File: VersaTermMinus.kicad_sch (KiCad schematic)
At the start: 55 parts, among them CN1 HDMI_A, CN2 DE15_Socket, CN3 USB_B_Micro, CN5 USB_B_Micro, CN6 Mini-DIN-6, CN7 TTL Serial, CN8 DE9 Socket, J2 USBDATA, Q1 2N7002, Q2 2N7002, Q3 2N7002, Q4 2N7002, Q5 2N7002, Q6 2N7002, Q7 2N7002, SW1 RESET, SW2 DEFAULTS, SW3 3V3/5V, U1 Raspberry Pi Pico, U3 MAX3232

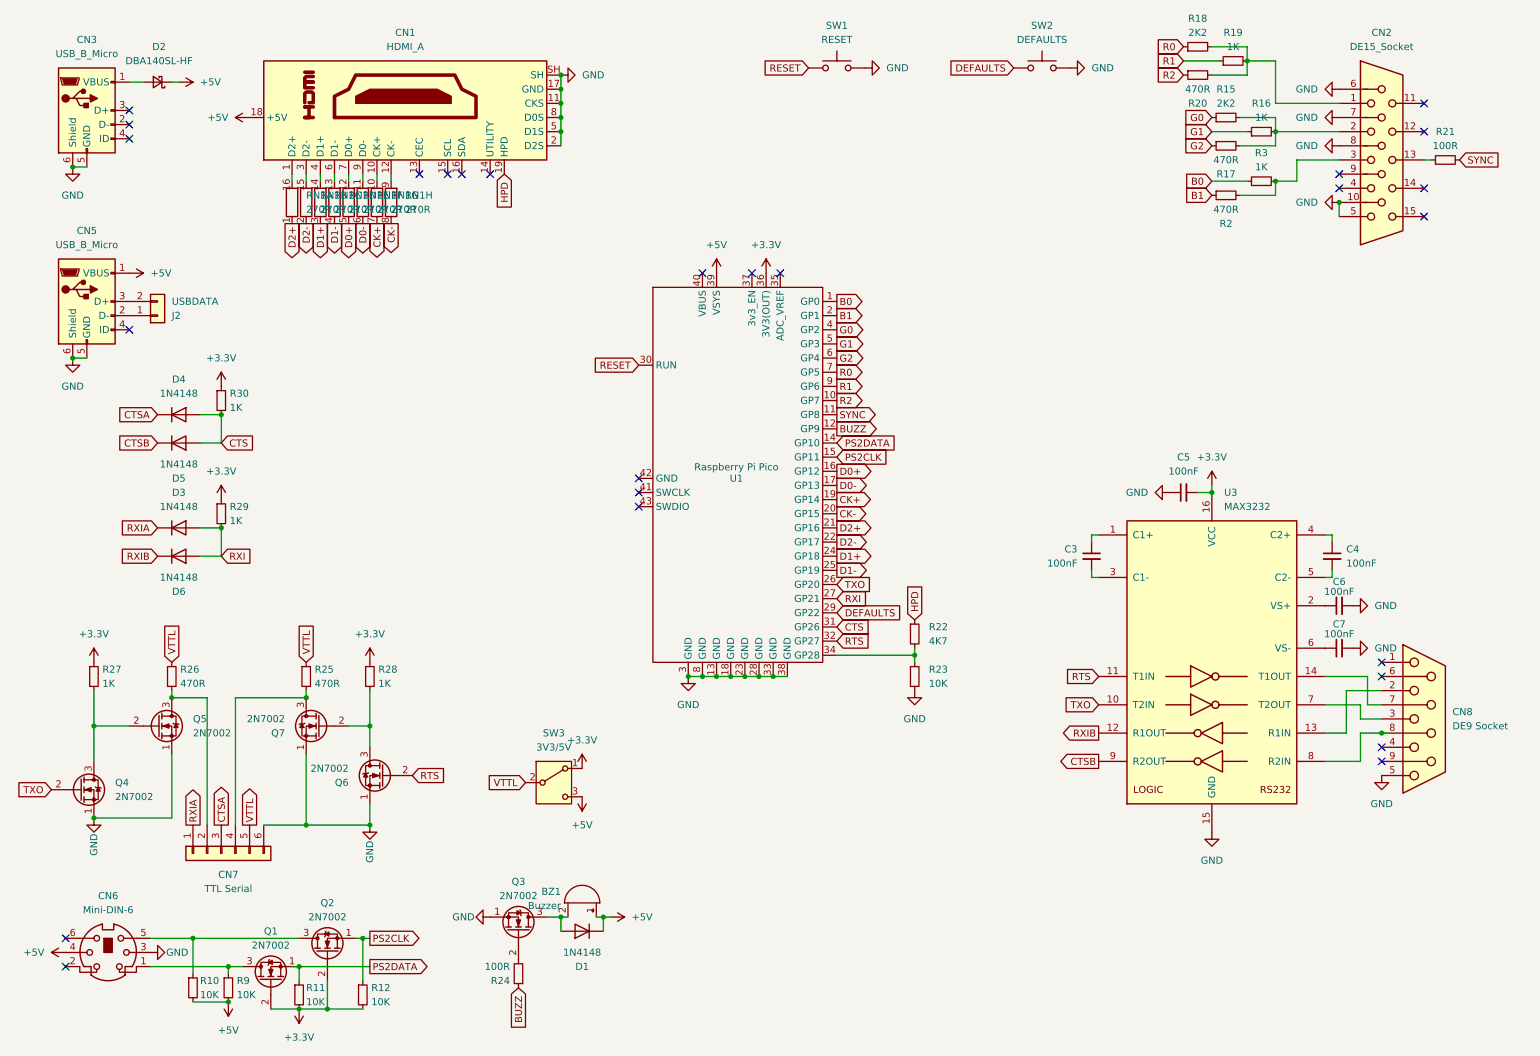
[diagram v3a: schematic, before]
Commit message: fix incorrect schema symbols for 2n7002 transistors
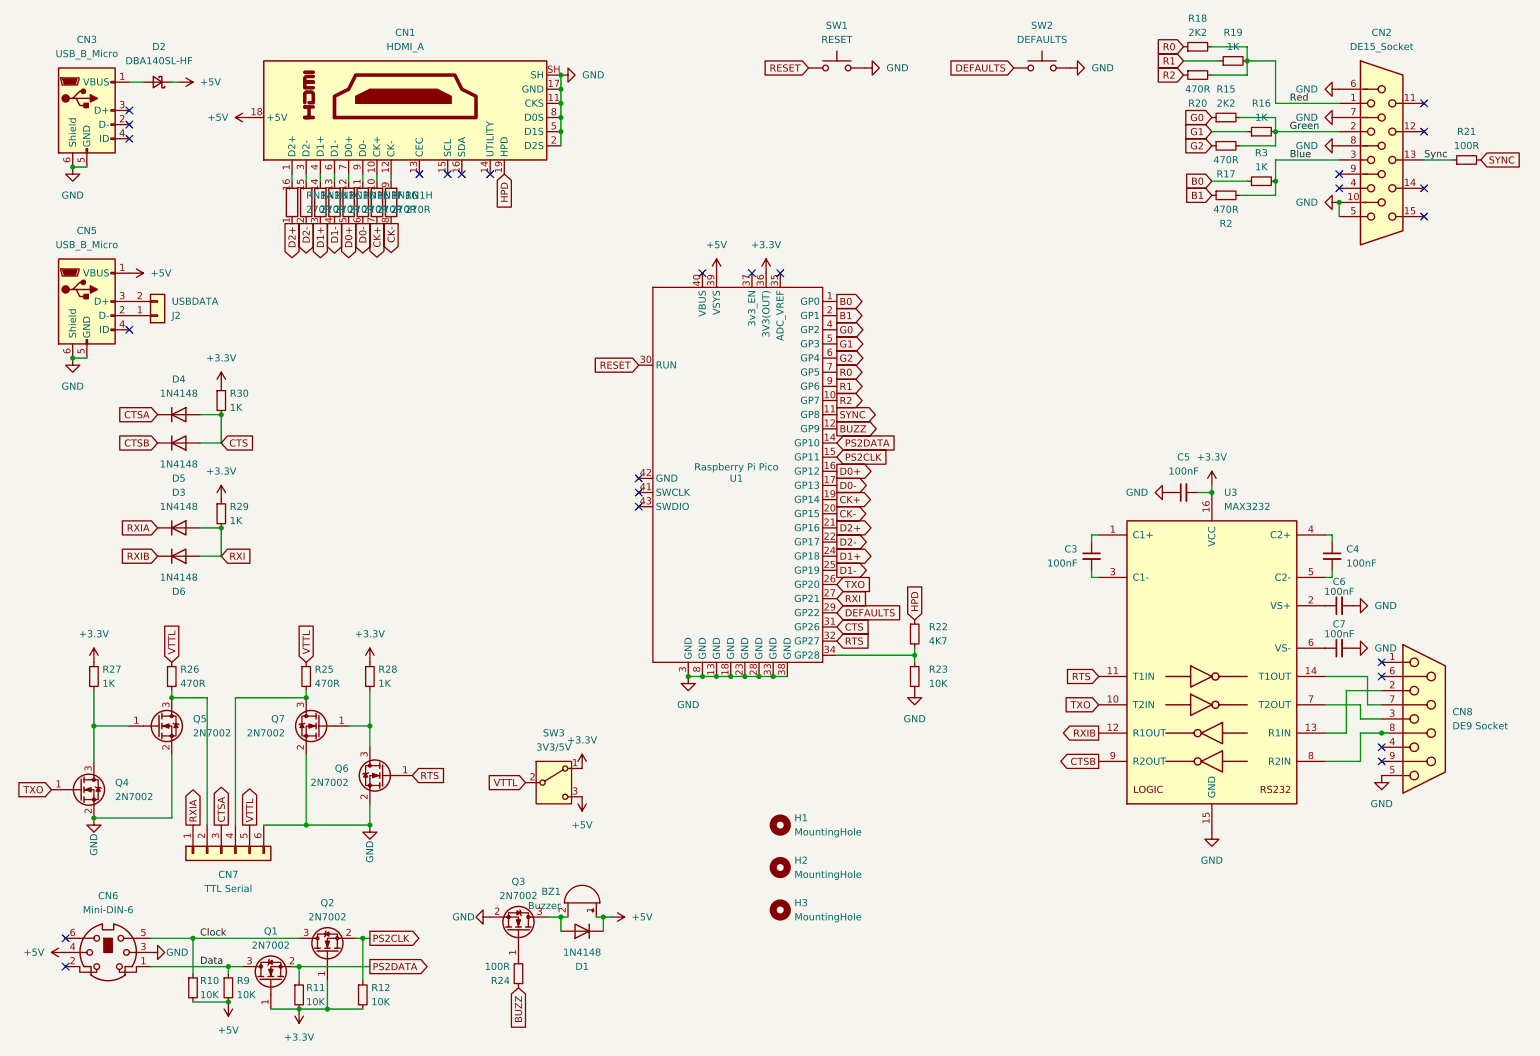
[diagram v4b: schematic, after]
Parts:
- removed Q1, Q2, Q3, Q4, Q5, Q6, Q7: 2N7002, Package_TO_SOT_SMD:SOT-23-3, symbol Transistor_FET:2N7000
- added H1, H2, H3: MountingHole, MountingHole:MountingHole_3.2mm_M3, symbol Mechanical:MountingHole
- added Q1, Q2, Q3, Q4, Q5, Q6, Q7: 2N7002, Package_TO_SOT_SMD:SOT-23, symbol Transistor_FET:2N7002
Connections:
- net +3.3V: now also Q1.1 (G), Q2.1 (G)
- net GND: now also Q3.2 (S), Q4.2 (S), Q5.2 (S), Q6.2 (S), Q7.2 (S)
- net PS2CLK: now also Q2.2 (S)
- net PS2DATA: now also Q1.2 (S)
- net RTS: now also Q6.1 (G)
- net TXO: now also Q4.1 (G)
- net Red: now reaches CN2.1, R18.2, R19.2, R20.2
- net at CN7.2 (Pin_2), R26.2: now also Q5.3 (D)
- net Data: now reaches CN6.1, R9.1
- net Data: now also Q1.3 (D)
- net Green: now reaches CN2.2, R15.2, R16.2, R17.2
- net at BZ1.2 (-), D1.2 (A): now also Q3.3 (D)
- net Sync: now reaches CN2.13, R21.1
- net at R27.2: now also Q4.3 (D), Q5.1 (G)
- net at R24.2: now also Q3.1 (G)
- net Clock: now reaches CN6.5, R10.1
- net Clock: now also Q2.3 (D)
- net Blue: now reaches CN2.3, R2.2, R3.2
- net at R28.2: now also Q6.3 (D), Q7.1 (G)
- net at CN7.4 (Pin_4), R25.2: now also Q7.3 (D)
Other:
- moved on the sheet: R21

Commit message: version 1.1
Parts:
- removed CN5: USB_B_Micro, Connector_USB:USB_Micro-B_Wuerth_629105150521, symbol Connector:USB_B_Micro
- added CN5: USB-A, Connector_USBA_Molex:CONN_67643-2911_MOL, symbol Connector_USBA_Molex:676432911
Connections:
- net +5V: now also CN6.3, CN5.1 (+5V); no longer CN6.4
- net Clock: now also CN6.6; no longer CN6.5
- net Data: now also CN6.2; no longer CN6.1
- net GND: now also CN6.4, CN5.4 (GND), CN5.5 (Shield); no longer CN6.3
- net at J2.1 (Pin_1): now also CN5.2 (D-)
- net at J2.2 (Pin_2): now also CN5.3 (D+)
- no-connect marks 26 -> 25
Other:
- moved on the sheet: J2
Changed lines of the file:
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@@
 	(generator_version "8.0")
 	(paper "A4")
+	(title_block
+		(date "2024-09-05")
+	)
 	(junction
 		(at 111.76 22.86)
@@
 	)
 	(junction
-		(at 66.04 134.62)
+		(at 29.21 67.31)
 		(diameter 0)
 		(color 0 0 0 0)
 	)
 	(junction
-		(at 41.91 134.62)
+		(at 66.04 134.62)
 		(diameter 0)
 		(color 0 0 0 0)
 	)
 	(junction
-		(at 111.76 173.99)
+		(at 41.91 134.62)
 		(diameter 0)
 		(color 0 0 0 0)
 	)
 	(junction
-		(at 24.13 73.66)
+		(at 111.76 173.99)
 		(diameter 0)
 		(color 0 0 0 0)
@@
 	)
 	(no_connect
-		(at 34.29 68.58)
-	)
-	(no_connect
 		(at 86.36 40.64)
 	)
@@
 	(wire
 		(pts
+			(xy 29.21 67.31) (xy 40.64 67.31)
+		)
+		(stroke
+			(width 0)
+			(type default)
+		)
+	)
+	(wire
+		(pts
 			(xy 250.19 105.41) (xy 250.19 106.68)
 		)
@@
 	(wire
 		(pts
+			(xy 40.64 62.23) (xy 40.64 67.31)
+		)
+		(stroke
+			(width 0)
+			(type default)
+		)
+	)
+	(wire
+		(pts
 			(xy 207.01 113.03) (xy 208.28 113.03)
 		)
@@
 	(wire
 		(pts
-			(xy 24.13 73.66) (xy 26.67 73.66)
-		)
-		(stroke
-			(width 0)
-			(type default)
-		)
-	)
-	(wire
-		(pts
 			(xy 255.27 146.05) (xy 255.27 140.97)
 		)
@@
 		)
 	)
+	(text_box "Note: supplied footprint has pins reversed compared to expected PS-2 socket"
+		(exclude_from_sim no)
+		(at 18.288 187.198 0)
+		(size 24.384 8.89)
+		(stroke
+			(width 0)
+			(type default)
+		)
+		(fill
+			(type none)
+		)
+		(effects
+			(font
+				(size 1.27 1.27)
+			)
+			(justify left top)
+		)
+	)
 	(label "Blue"
 		(at 242.57 38.1 0)
@@
 	)
 	(symbol
-		(lib_id "Connector:USB_B_Micro")
-		(at 26.67 63.5 0)
-		(unit 1)
-		(exclude_from_sim no)
-		(in_bom yes)
-		(on_board yes)
-		(dnp no)
-		(fields_autoplaced yes)
-		(property "Reference" "CN5"
-			(at 26.67 50.8 0)
-			(effects
-				(font
-					(size 1.27 1.27)
-				)
-			)
-		)
-		(property "Value" "USB_B_Micro"
-			(at 26.67 53.34 0)
-			(effects
-				(font
-					(size 1.27 1.27)
-				)
-			)
-		)
-		(property "Footprint" "Connector_USB:USB_Micro-B_Wuerth_629105150521"
-			(at 30.48 64.77 0)
-			(effects
-				(font
-					(size 1.27 1.27)
-				)
-				(hide yes)
-			)
-		)
-		(property "Datasheet" "https://www.we-online.com/katalog/datasheet/629105150521.pdf"
-			(at 30.48 64.77 0)
-			(effects
-				(font
-					(size 1.27 1.27)
-				)
-				(hide yes)
-			)
-		)
-		(property "Description" "USB Micro Type B connector"
-			(at 26.67 63.5 0)
-			(effects
-				(font
-					(size 1.27 1.27)
-				)
-				(hide yes)
-			)
-		)
-		(property "DigiKey" "732-5960-1-ND"
-			(at 26.67 63.5 0)
-			(effects
-				(font
-					(size 1.27 1.27)
-				)
-				(hide yes)
-			)
-		)
-		(pin "3"
-		)
-		(pin "4"
-		)
-		(pin "6"
-		)
-		(pin "5"
-		)
-		(pin "1"
-		)
-		(pin "2"
-		)
-		(instances
-			(project "VersaTermMinus"
-				(path "/6aa9664d-1ced-4a58-b8c7-aff67171855f"
-					(reference "CN5")
-					(unit 1)
-				)
-			)
-		)
-	)
-	(symbol
 		(lib_id "Diode:1N4148")
 		(at 43.18 83.82 0)
@@
 		(lib_id "Connector:Mini-DIN-6")
 		(at 30.48 180.34 0)
+		(mirror y)
 		(unit 1)
 		(exclude_from_sim no)
@@
 		(on_board yes)
 		(dnp no)
-		(fields_autoplaced yes)
 		(property "Reference" "CN6"
-			(at 30.4977 170.18 0)
+			(at 30.4623 170.18 0)
 			(effects
 				(font
@@
 		)
 		(property "Value" "Mini-DIN-6"
-			(at 30.4977 172.72 0)
+			(at 30.4623 172.72 0)
 			(effects
 				(font
@@
 	)
 	(symbol
+		(lib_id "Connector_USBA_Molex:676432911")
+		(at 38.1 54.61 0)
+		(mirror y)
+		(unit 1)
+		(exclude_from_sim no)
+		(in_bom yes)
+		(on_board yes)
+		(dnp no)
+		(property "Reference" "CN5"
+			(at 26.67 57.1499 0)
+			(effects
+				(font
+					(size 1.524 1.524)
+				)
+				(justify left)
+			)
+		)
+		(property "Value" "USB-A"
+			(at 26.67 59.6899 0)
+			(effects
+				(font
+					(size 1.524 1.524)
+				)
+				(justify left)
+			)
+		)
+		(property "Footprint" "Connector_USBA_Molex:CONN_67643-2911_MOL"
+			(at 38.354 45.212 0)
+			(effects
+				(font
+					(size 1.27 1.27)
+					(italic yes)
+				)
+				(hide yes)
+			)
+		)
+		(property "Datasheet" "676432911"
+			(at 38.1 47.498 0)
+			(effects
+				(font
+					(size 1.27 1.27)
+					(italic yes)
+				)
+				(hide yes)
+			)
+		)
+		(property "Description" ""
+			(at 40.64 54.61 0)
+			(effects
+				(font
+					(size 1.27 1.27)
+				)
+				(hide yes)
+			)
+		)
+		(property "DigiKey" "WM4078-ND"
+			(at 38.1 54.61 0)
+			(effects
+				(font
+					(size 1.27 1.27)
+				)
+				(hide yes)
+			)
+		)
+		(pin "5"
+		)
+		(pin "2"
+		)
+		(pin "4"
+		)
+		(pin "3"
+		)
+		(pin "1"
+		)
+		(instances
+			(project ""
+				(path "/6aa9664d-1ced-4a58-b8c7-aff67171855f"
+					(reference "CN5")
+					(unit 1)
+				)
+			)
+		)
+	)
+	(symbol
 		(lib_id "Device:R_Small")
 		(at 231.14 30.48 90)
@@
 	(symbol
 		(lib_id "Connector_Generic:Conn_01x02")
-		(at 39.37 66.04 0)
-		(mirror x)
+		(at 45.72 57.15 0)
 		(unit 1)
 		(exclude_from_sim no)
@@
 		(dnp no)
 		(property "Reference" "J2"
-			(at 41.91 66.0401 0)
+			(at 48.26 57.1499 0)
 			(effects
 				(font
@@
 		)
 		(property "Value" "USBDATA"
-			(at 41.91 63.5001 0)
+			(at 48.26 59.6899 0)
 			(effects
 				(font
@@
 		)
 		(property "Footprint" "Connector_PinHeader_2.54mm:PinHeader_1x02_P2.54mm_Vertical"
-			(at 39.37 66.04 0)
+			(at 45.72 57.15 0)
 			(effects
 				(font
@@
 		)
 		(property "Datasheet" "~"
-			(at 39.37 66.04 0)
+			(at 45.72 57.15 0)
 			(effects
 				(font
@@
 		)
 		(property "Description" "Generic connector, single row, 01x02, script generated (kicad-library-utils/schlib/autogen/connector/)"
-			(at 39.37 66.04 0)
+			(at 45.72 57.15 0)
 			(effects
 				(font
@@
 	(symbol
 		(lib_id "power:GND")
-		(at 24.13 73.66 0)
+		(at 29.21 67.31 0)
 		(unit 1)
 		(exclude_from_sim no)
@@
 		(fields_autoplaced yes)
 		(property "Reference" "#PWR028"
-			(at 24.13 80.01 0)
+			(at 29.21 73.66 0)
 			(effects
 				(font
@@
 		)
 		(property "Value" "GND"
-			(at 24.13 78.74 0)
+			(at 29.21 72.39 0)
 			(effects
 				(font
@@
 		)
 		(property "Footprint" ""
-			(at 24.13 73.66 0)
+			(at 29.21 67.31 0)
 			(effects
 				(font
@@
 		)
 		(property "Datasheet" ""
-			(at 24.13 73.66 0)
+			(at 29.21 67.31 0)
 			(effects
 				(font
@@
 		)
 		(property "Description" "Power symbol creates a global label with name \"GND\" , ground"
-			(at 24.13 73.66 0)
+			(at 29.21 67.31 0)
 			(effects
 				(font
@@
 	(symbol
 		(lib_id "power:+5V")
-		(at 34.29 58.42 270)
+		(at 40.64 54.61 270)
 		(unit 1)
 		(exclude_from_sim no)
@@
 		(fields_autoplaced yes)
 		(property "Reference" "#PWR027"
-			(at 30.48 58.42 0)
+			(at 36.83 54.61 0)
 			(effects
 				(font
@@
 		)
 		(property "Value" "+5V"
-			(at 38.1 58.4199 90)
+			(at 44.45 54.6099 90)
 			(effects
 				(font
@@
 		)
 		(property "Footprint" ""
-			(at 34.29 58.42 0)
+			(at 40.64 54.61 0)
 			(effects
 				(font
@@
 		)
 		(property "Datasheet" ""
-			(at 34.29 58.42 0)
+			(at 40.64 54.61 0)
 			(effects
 				(font
@@
 		)
 		(property "Description" "Power symbol creates a global label with name \"+5V\""
-			(at 34.29 58.42 0)
+			(at 40.64 54.61 0)
 			(effects
 				(font

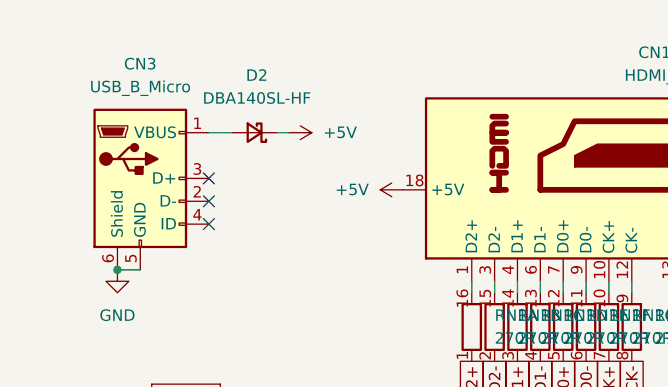
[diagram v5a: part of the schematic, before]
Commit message: add TP labels to back silkscreen
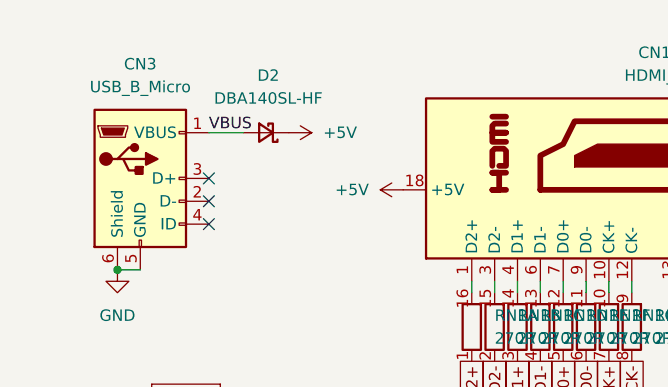
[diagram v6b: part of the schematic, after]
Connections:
- net VBUS: now reaches CN3.1 (VBUS), D2.2 (A)
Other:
- moved on the sheet: D2
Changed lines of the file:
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@@
 	(wire
 		(pts
-			(xy 36.83 24.13) (xy 34.29 24.13)
+			(xy 38.1 24.13) (xy 34.29 24.13)
 		)
 		(stroke
@@
 	(wire
 		(pts
-			(xy 41.91 24.13) (xy 43.18 24.13)
-		)
-		(stroke
-			(width 0)
-			(type default)
-		)
-	)
-	(wire
-		(pts
 			(xy 142.24 130.81) (xy 144.78 130.81)
 		)
@@
 	(label "Blue"
 		(at 242.57 38.1 0)
-		(fields_autoplaced yes)
 		(effects
 			(font
@@
 	(label "Green"
 		(at 242.57 33.02 0)
-		(fields_autoplaced yes)
+		(effects
+			(font
+				(size 1.27 1.27)
+			)
+			(justify left bottom)
+		)
+	)
+	(label "VBUS"
+		(at 34.29 24.13 0)
 		(effects
 			(font
@@
 	(label "Clock"
 		(at 46.99 177.8 0)
-		(fields_autoplaced yes)
 		(effects
 			(font
@@
 	(label "Sync"
 		(at 266.7 38.1 0)
-		(fields_autoplaced yes)
 		(effects
 			(font
@@
 	(label "Red"
 		(at 242.57 27.94 0)
-		(fields_autoplaced yes)
 		(effects
 			(font
@@
 	(label "Data"
 		(at 46.99 182.88 0)
-		(fields_autoplaced yes)
 		(effects
 			(font
@@
 	(symbol
 		(lib_id "Device:D_Schottky_Small")
-		(at 39.37 24.13 180)
+		(at 40.64 24.13 180)
 		(unit 1)
 		(exclude_from_sim no)
@@
 		(fields_autoplaced yes)
 		(property "Reference" "D2"
-			(at 39.624 17.78 0)
+			(at 40.894 17.78 0)
 			(effects
 				(font
@@
 		)
 		(property "Value" "DBA140SL-HF"
-			(at 39.624 20.32 0)
+			(at 40.894 20.32 0)
 			(effects
 				(font
@@
 		)
 		(property "Footprint" "Diode_SMD:D_SMA_Handsoldering"
-			(at 39.37 24.13 90)
+			(at 40.64 24.13 90)
 			(effects
 				(font
@@
 		)
 		(property "Datasheet" "~"
-			(at 39.37 24.13 90)
+			(at 40.64 24.13 90)
 			(effects
 				(font
@@
 		)
 		(property "Description" "Schottky diode, small symbol"
-			(at 39.37 24.13 0)
+			(at 40.64 24.13 0)
 			(effects
 				(font
@@
 		)
 		(property "DigiKey" "641-1762-1-ND"
-			(at 39.37 24.13 0)
+			(at 40.64 24.13 0)
 			(effects
 				(font
